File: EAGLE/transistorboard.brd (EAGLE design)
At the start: 16.5 x 28.9 mm, 5 parts, among them T1 BC337

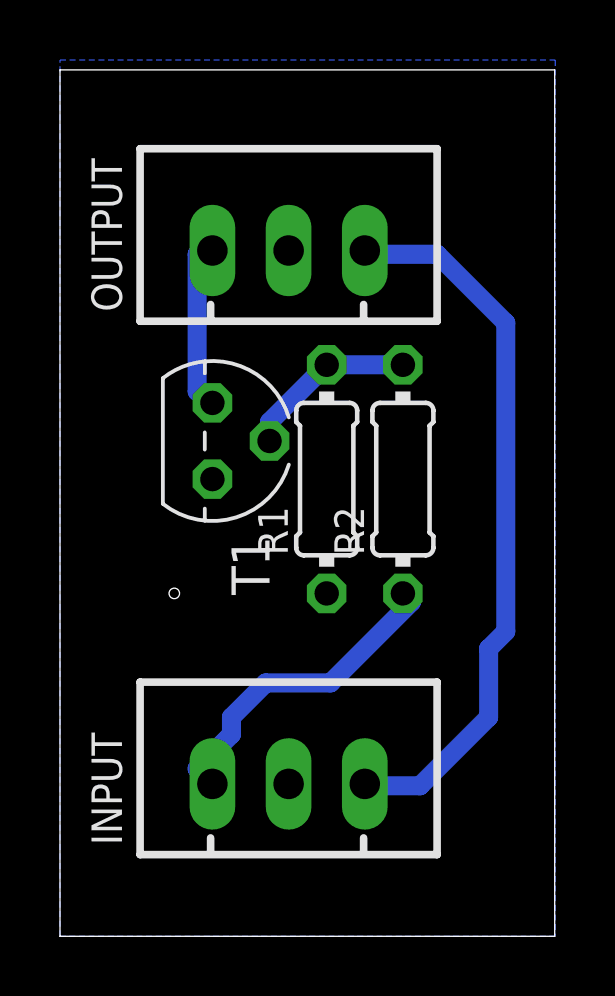
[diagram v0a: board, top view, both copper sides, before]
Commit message: * Moved all EAGLE files into the project * Removed old copy-pasted boards * Updated .gitignore
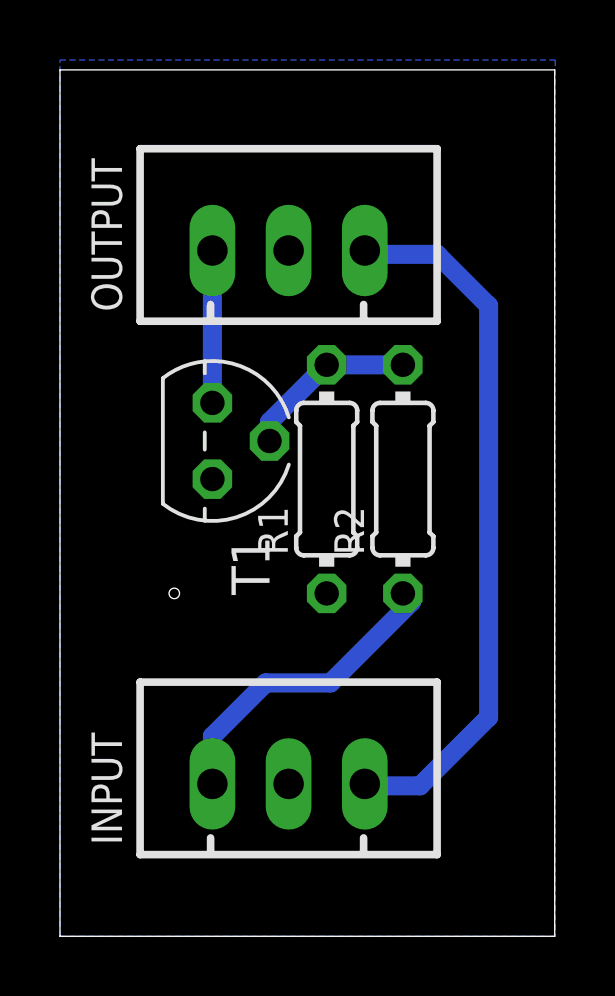
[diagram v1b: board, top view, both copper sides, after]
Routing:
- net N$1: track 5.73 -> 5.08 mm
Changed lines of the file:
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@@
 <wire x1="12.0015" y1="5.0165" x2="10.287" y2="5.0165" width="0.635" layer="16"/>
 <wire x1="14.2875" y1="7.3025" x2="12.0015" y2="5.0165" width="0.635" layer="16"/>
-<wire x1="14.2875" y1="9.5885" x2="14.2875" y2="7.3025" width="0.635" layer="16"/>
-<wire x1="14.859" y1="10.16" x2="14.2875" y2="9.5885" width="0.635" layer="16"/>
-<wire x1="14.859" y1="20.447" x2="14.859" y2="10.16" width="0.635" layer="16"/>
-<wire x1="12.573" y1="22.733" x2="14.859" y2="20.447" width="0.635" layer="16"/>
+<wire x1="14.2875" y1="21.0185" x2="14.2875" y2="7.3025" width="0.635" layer="16"/>
+<wire x1="12.573" y1="22.733" x2="14.2875" y2="21.0185" width="0.635" layer="16"/>
 <wire x1="10.287" y1="22.733" x2="12.573" y2="22.733" width="0.635" layer="16"/>
 <wire x1="10.287" y1="5.0165" x2="10.16" y2="5.08" width="0.635" layer="16"/>
@@
 <wire x1="9.017" y1="8.4455" x2="11.71575" y2="11.14425" width="0.635" layer="16"/>
 <wire x1="6.858" y1="8.4455" x2="9.017" y2="8.4455" width="0.635" layer="16"/>
-<wire x1="5.715" y1="7.3025" x2="6.858" y2="8.4455" width="0.635" layer="16"/>
-<wire x1="5.715" y1="6.731" x2="5.715" y2="7.3025" width="0.635" layer="16"/>
-<wire x1="4.572" y1="5.588" x2="5.715" y2="6.731" width="0.635" layer="16"/>
+<wire x1="6.858" y1="8.4455" x2="5.08" y2="6.6675" width="0.635" layer="16"/>
+<wire x1="5.08" y1="5.08" x2="5.08" y2="6.6675" width="0.635" layer="16"/>
 <wire x1="11.71575" y1="11.14425" x2="11.43" y2="11.43" width="0.635" layer="16"/>
-<wire x1="4.572" y1="5.588" x2="5.08" y2="5.08" width="0.635" layer="16"/>
 </signal>
 <signal name="N$1">
 <contactref element="OUTPUT" pad="1"/>
 <contactref element="T1" pad="3"/>
-<wire x1="4.572" y1="22.733" x2="4.572" y2="18.161" width="0.635" layer="16"/>
-<wire x1="4.572" y1="18.161" x2="5.08" y2="17.78" width="0.635" layer="16"/>
-<wire x1="4.572" y1="22.733" x2="5.08" y2="22.86" width="0.635" layer="16"/>
+<wire x1="5.08" y1="17.78" x2="5.08" y2="22.86" width="0.635" layer="16"/>
 </signal>
 <signal name="N$4">
